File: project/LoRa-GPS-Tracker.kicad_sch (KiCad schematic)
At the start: 63 parts, among them IC101 MCP73831-2-OT, IC102 MCP100T-300I/TT, IC103 FT230XS, IC104 NCP705MT30TCG, IC105 LIS2DH, M101 SIM28ML, M102 RAK3172, Q101 BSS84, Q102 BSH205G2VL, Q103 BSS123, Q104 BSS84, SW101 ON/OFF, X101 DEBUG, X102 Conn_Coaxial, X103 BATTERY, X3 DEBUG

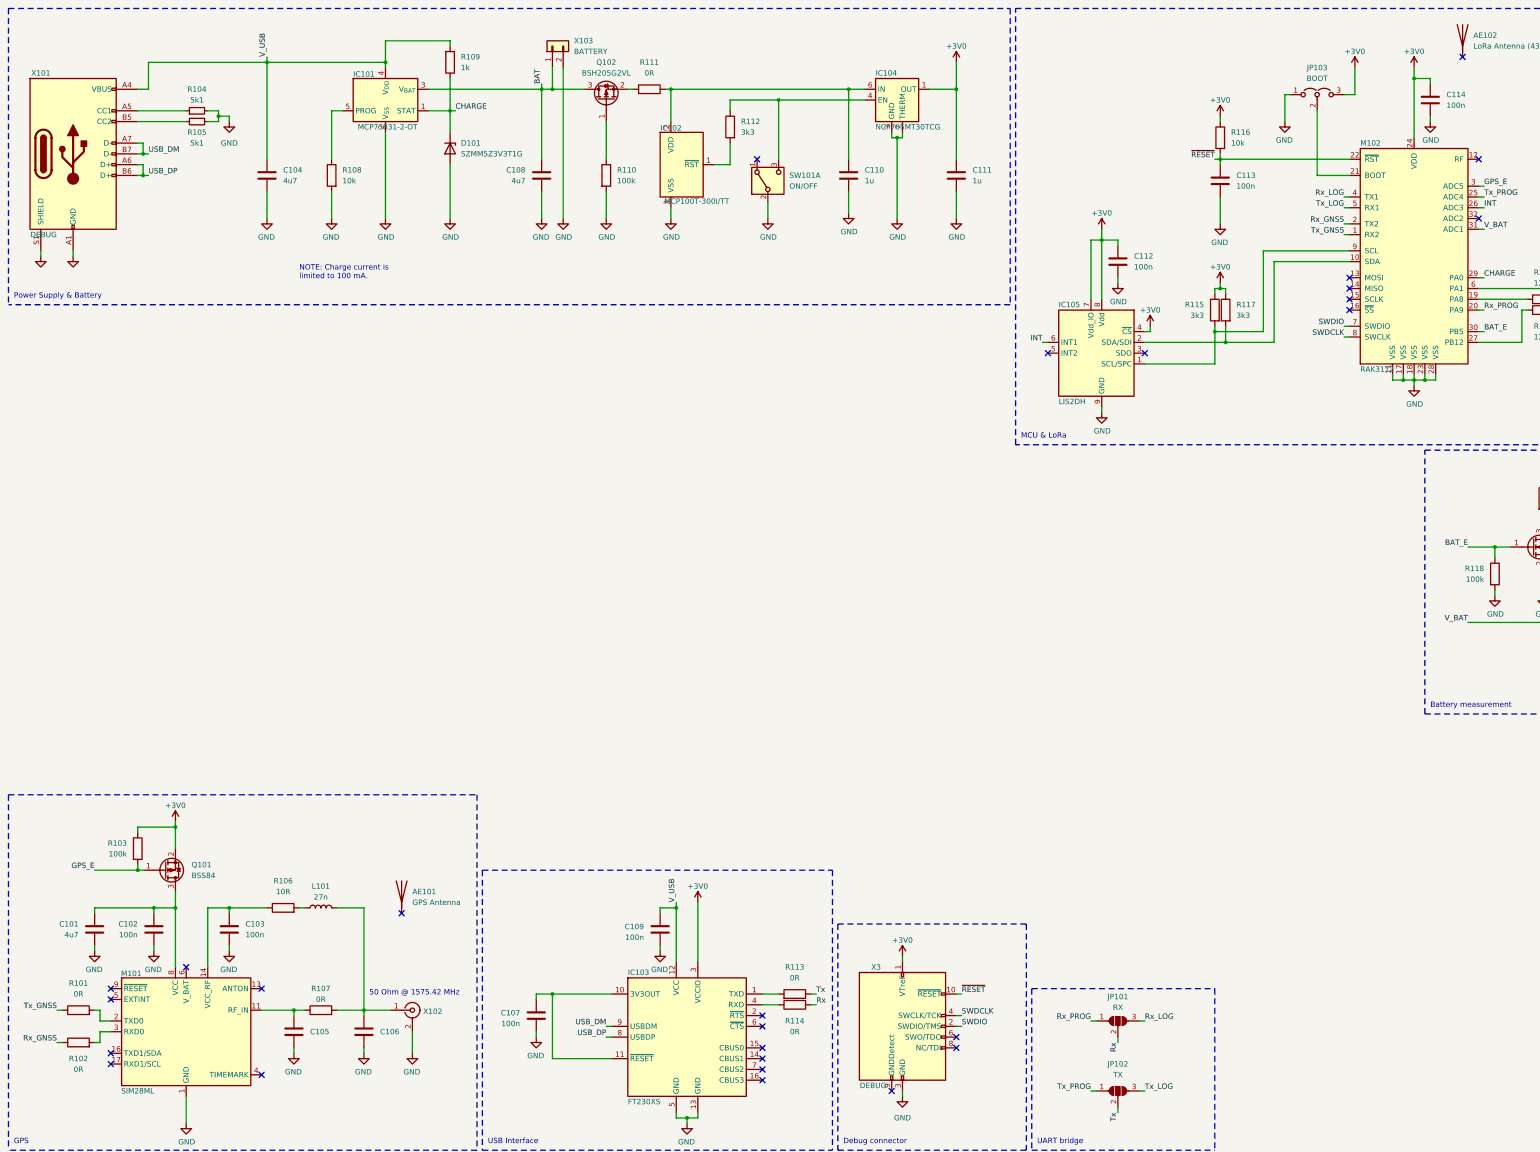
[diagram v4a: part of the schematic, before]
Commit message: Fix wrong footprint for status LED
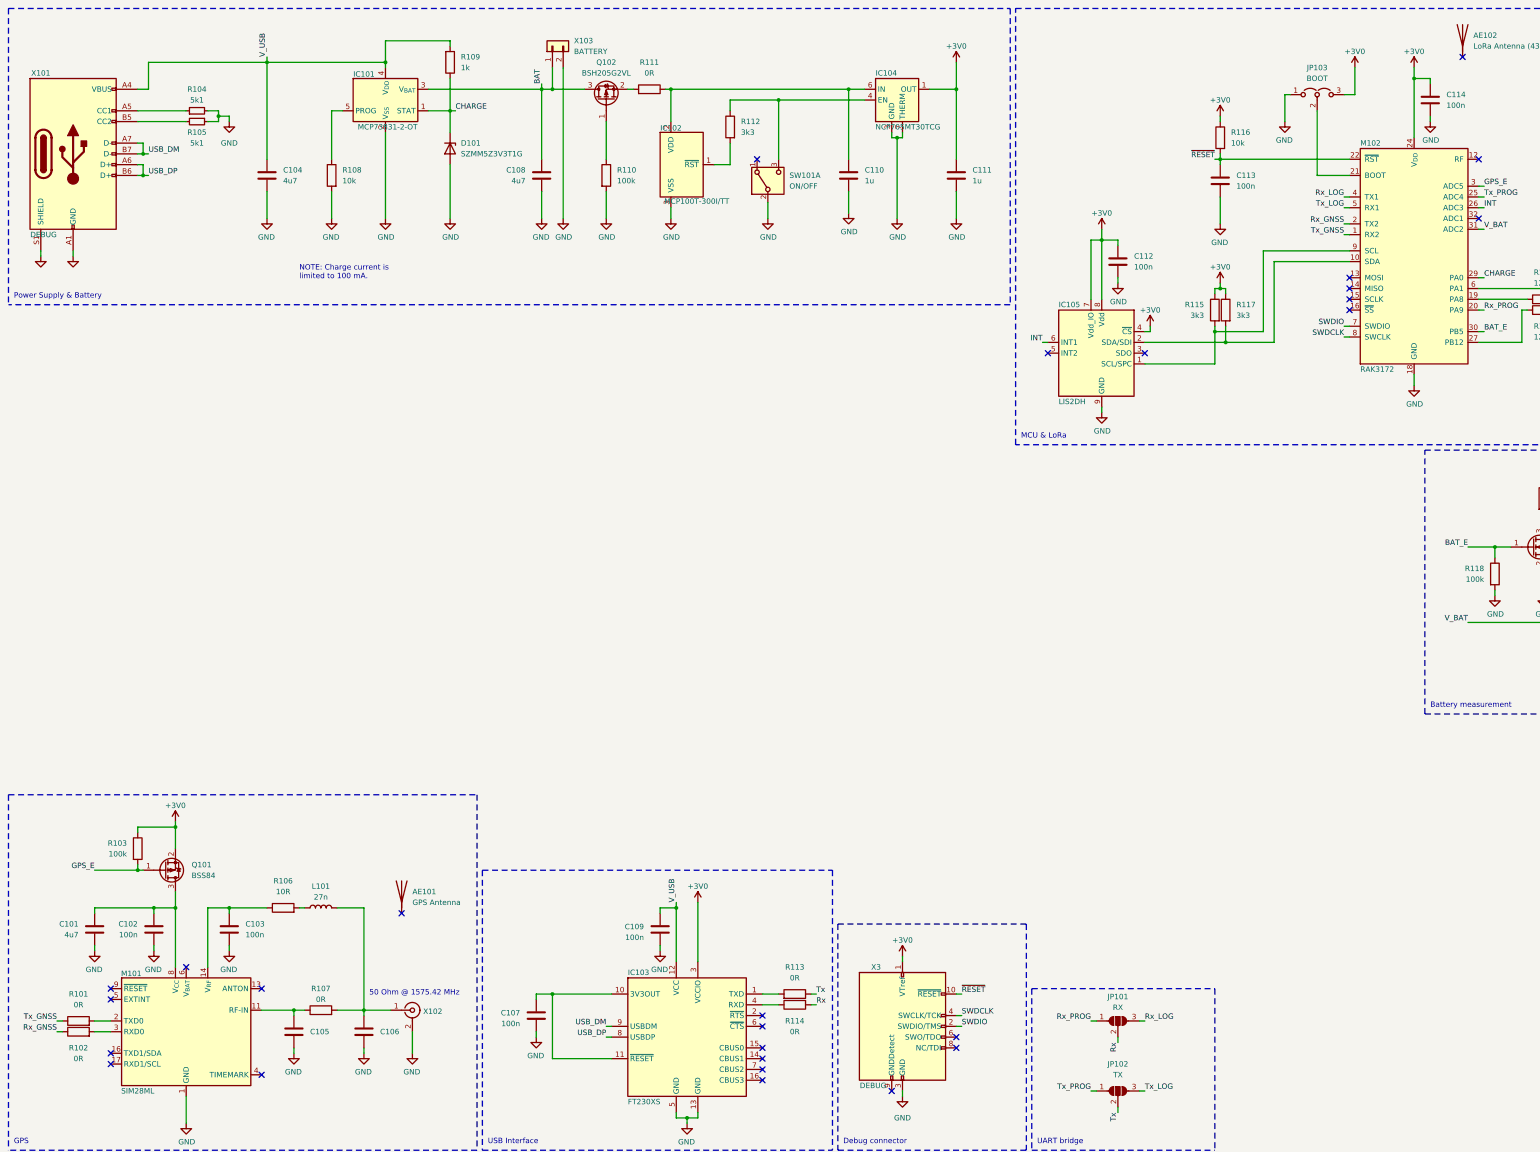
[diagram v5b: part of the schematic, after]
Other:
- moved on the sheet: R101, R102
